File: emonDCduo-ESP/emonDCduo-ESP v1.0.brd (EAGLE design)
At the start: 99.1 x 76.5 mm, 85 parts, among them Q1 16Mhz XT49M-2016M, U1_TQFP ATMEGA328P

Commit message: updating v1.0
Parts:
- removed GPIO-4/5: (no value), SparkFun:1X02
- removed REFERENCE_SELECT: 2212S-02SG-85, SparkFun-Connectors:1X03
- removed U$1: 47219-2001_MICROSD, 47219-2001_SD_MICRO:47219-2001_MICROSD
- added GPIO5: (no value), wirepad:2,15/1,0
- added R9: 10k, rcl:R0603
- added REF_SELECT: 2212S-02SG-85, SparkFun-Connectors:1X03
- added U$2: MOLEX_MICRO_SD_1040310811, MOLEX MICRO SD [exposed pins]:MOLEX_MICROSD_EXPOSED
- REG1117: value REG1117 -> REG1117-3.3V
- TL2575HV: value TL2575HV -> TL2575HV-5V
- moved R24 2.79 mm to (79.8, 24.5)
- moved LOGO1 2.19 mm to (22.7, 15.8)
- moved C23 1.02 mm to (31.9, 56.6), turned to 0 degrees
- moved R3 0.96 mm to (42.2, 23.0), turned to 0 degrees
- moved C10 0.56 mm to (21.3, 70.1)
- moved R10 0.25 mm to (83.5, 41.9)
- renumbered 3.3V_REG to REG1117, 5V_REG to TL2575HV, C20/TUNE to C20, JP3 to JP_PWR
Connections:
- removed net N$28: REFERENCE_SELECT.2, SHUNTMON-A.6, SHUNTMON-A.7
- new net N$10: R9.2, U$2.CD1
- new net N$11: REF_SELECT.2, SHUNTMON-A.6, SHUNTMON-A.7
- net 3.3V: now also U$2.P$4; no longer U$1.PIN4
- net GND: now also REF_SELECT.3, U$2.CD2, U$2.GND1, U$2.GND2, U$2.GND3, U$2.GND4, U$2.P$6; no longer REFERENCE_SELECT.3, U$1.P$1, U$1.P$2, U$1.P$3, U$1.P$4, U$1.PIN6
- net GPIO12: now also U$2.P$7; no longer U$1.PIN7
- net GPIO13: now also U$2.P$3; no longer U$1.PIN3
- net GPIO14: now also U$2.P$5; no longer U$1.PIN5
- net GPIO2: now also U$2.P$2; no longer U$1.PIN2
- net GPIO4: now also R9.1; no longer GPIO-4/5.1
- net GPIO5: now also GPIO5.1; no longer GPIO-4/5.2
- net N$32: now also U$2.P$8; no longer U$1.PIN8
- net N$7: now also U$2.P$1; no longer U$1.PIN1
- net REFINPUT: now also REF_SELECT.1; no longer REFERENCE_SELECT.1
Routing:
- net GND: track 3.81 -> 52.3 mm, vias 54 -> 57
- net N$11: track 0.00 -> 21.4 mm, vias 0 -> 1
- net N$28: track 18.5 -> 0.00 mm, vias 1 -> 0
- net N$10: track 0.00 -> 15.8 mm, vias 0 -> 2
- net REFINPUT: track 19.4 -> 24.3 mm
- net GPIO14: track 54.8 -> 59.4 mm
- net GPIO12: track 53.6 -> 58.2 mm
- net GPIO13: track 64.9 -> 69.1 mm
- net 3.3V: track 267.5 -> 264.0 mm
- net 4.7V: track 163.5 -> 166.6 mm
- net GPIO5: track 32.0 -> 29.1 mm
- net GPIO2: track 50.0 -> 52.5 mm
- net POWERIN: track 33.6 -> 34.4 mm
- net GPIO4: track 30.5 -> 29.9 mm
- net ESPRX: track 13.1 -> 13.6 mm
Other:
- board text added: "330uH"
- board text added: "BI_DIR"
- board text added: "MicroSD"
- board text added: "UNI_DIR"
- board text added: "v1.0 Feb 2017 by DB"
- board text removed: "GPIO4"
- board text removed: "GPIO5"
- board text removed: "MICRO SD"
- board text removed: "v0.4 Jan 2017 by DB"

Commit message: update
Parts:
- added GPIO1: (no value), SparkFun:1X02
- added MINI_USB-B: 5000751517_SD, 5000751517_sd:5000751517_SD
- D1: value BAT60J -> MBRA130LT3G; device diode:SOD323_ST -> CASE 403D Diode:DO-214
- D2: value MBRA130LT3G -> BAT60J; device CASE 403D Diode:DO-214 -> diode:SOD323_ST
- moved D1 26.0 mm to (46.9, 62.4), turned to 270 degrees
- moved D2 26.0 mm to (72.8, 65.6), turned to 180 degrees
- moved GPIO0 1.14 mm to (42.2, 29.0)
- moved C11 0.25 mm to (75.0, 35.8)
- moved C4 0.25 mm to (64.8, 35.8)
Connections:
- net 4.7V: now also D2.C, FTDI1.4, MINI_USB-B.VBUS; no longer D1.C
- net 5.0V: now also D2.A; no longer D1.A
- net GND: now also D1.P$2, GPIO1.1, MINI_USB-B.GND1, MINI_USB-B.GND2, MINI_USB-B.GND3; no longer D2.P$2
- net GPIO15: now also GPIO1.2
- net IND: now also D1.P$1; no longer D2.P$1
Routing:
- net 4.7V: track 166.6 -> 186.1 mm, vias 8 -> 9
- net GPIO15: track 26.6 -> 33.3 mm
- net N$36: track 33.7 -> 31.6 mm
- net GPIO0: track 18.5 -> 19.9 mm
- net GND: vias 57 -> 59
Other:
- board text added: "D1"
- board text added: "MINI USB-B"
- board text removed: "D2"

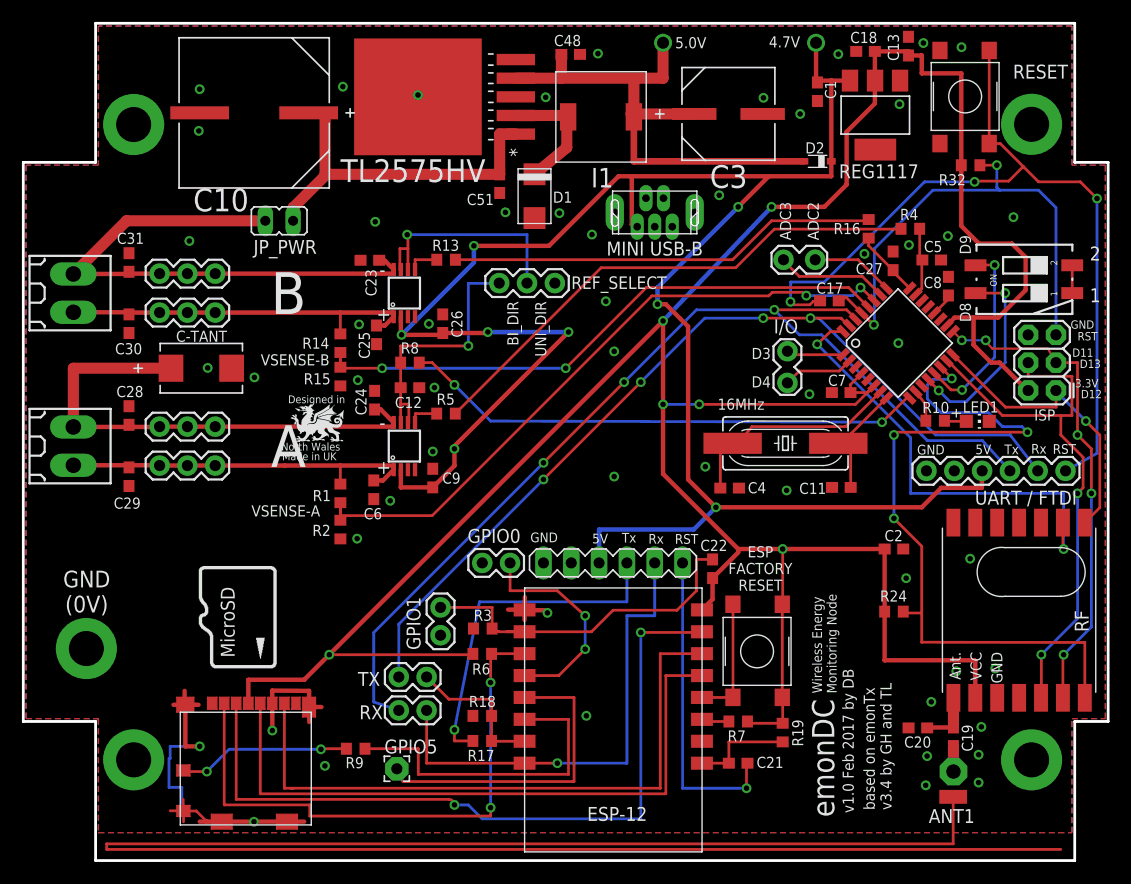
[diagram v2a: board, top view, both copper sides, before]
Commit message: added DIP switch to ESP RX/TX
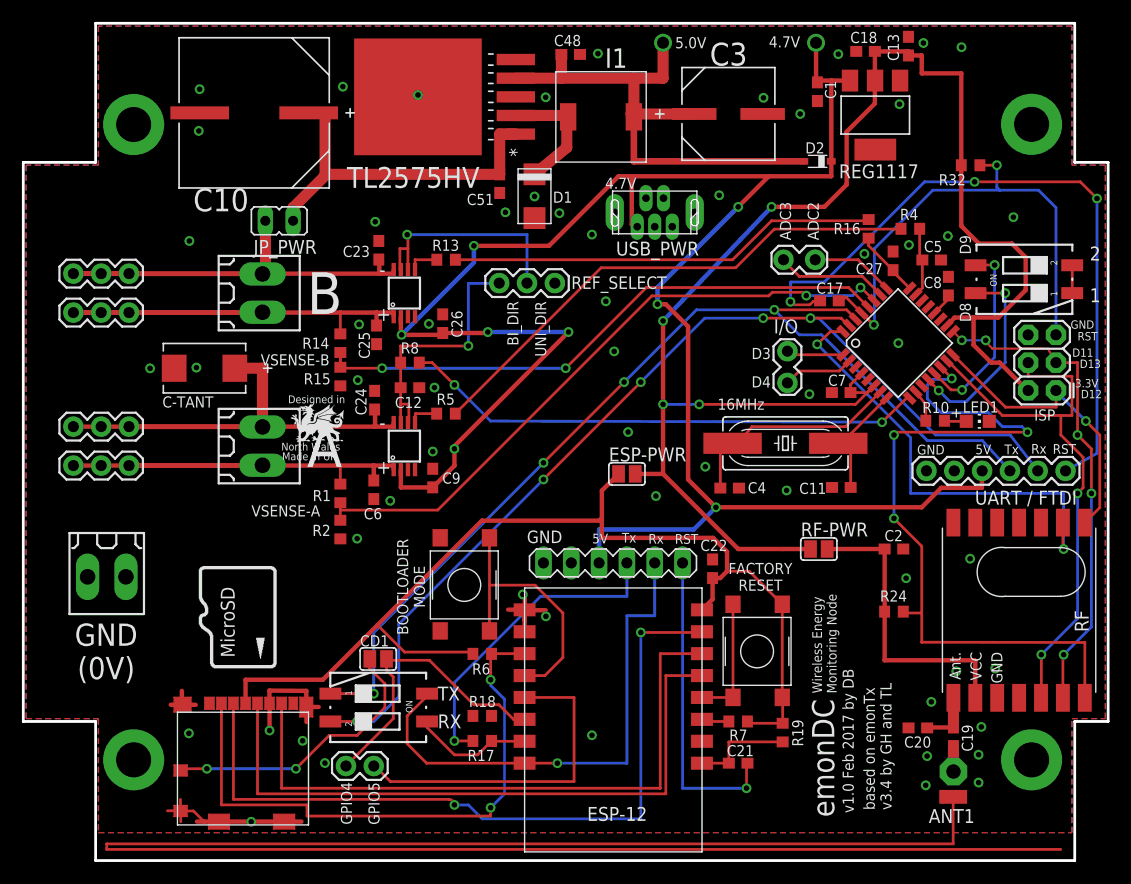
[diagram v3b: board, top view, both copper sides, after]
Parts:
- removed C28, C29, C30, C31: 0.1uF 100V, rcl:C0603
- removed GPIO0, GPIO1, RX, TX: (no value), SparkFun:1X02
- removed GPIO5: (no value), wirepad:2,15/1,0
- removed MC32882: MC32882, multicomp tact switch:SWITCH_TACT_MULTICOMP
- removed R3, R9: 10k, rcl:R0603
- added CD1, ESP-PWR, RF-PWR: (no value), jumper:SJ
- added IO2: (no value), SparkFun:1X02
- added MC2: MC32882, multicomp tact switch:SWITCH_TACT_MULTICOMP
- added S1: A6S-2104-PH, OpenEnergyMonitor:DIP_SWITCH_SMT
- added T3: (no value), con-weidmueller-sl35:180-2
- moved T1 17.3 mm to (22.1, 53.6)
- moved T2 17.3 mm to (22.1, 39.6)
- moved J1 7.87 mm to (4.83, 55.4)
- moved J2 7.87 mm to (4.83, 51.8)
- moved J3 7.87 mm to (4.83, 37.8)
- moved J4 7.87 mm to (4.83, 41.4)
- moved C23 1.22 mm to (32.7, 57.5), turned to 270 degrees
- moved C-TANT 0.29 mm to (16.8, 46.7), turned to 180 degrees
- moved U$2 0.25 mm to (20.0, 10.4)
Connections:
- net ADCVSENSE-A renamed ADC5-VSENSEB
- net ADCVSENSE-B renamed ADC4-VSENSEA
- net N$2 renamed ADC0
- net N$27 renamed ADC1
- removed net GPIO15: C22.1, ESP-12.1, ESP-12.2, GPIO1.2, R3.2
- new net 3.3V-ESP: C22.2, ESP-12.16, ESP-PWR.1, MC1.P$3, MC1.P$4, R19.2, R6.2, R7.2, U$2.P$4
- new net N$17: C2.1, R24.2, RF-PWR.2, RF.VDD
- net 3.3V: now also ESP-PWR.2, RF-PWR.1; no longer C2.1, C22.2, ESP-12.16, MC1.P$3, MC1.P$4, R19.2, R24.2, R6.2, R7.2, RF.VDD, U$2.P$4
- net ADCSHUNT-A: now also R4.2, R5.2; no longer R13.2, R16.2
- net ADCSHUNT-B: now also R13.2, R16.2; no longer R4.2, R5.2
- net D0/RX: now also S1.1; no longer RX.2
- net D1/TX: now also S1.2; no longer TX.2
- net ESPRX: now also S1.3; no longer TX.1
- net ESPTX: now also S1.4; no longer RX.1
- net GND: now also C22.1, ESP-12.1, ESP-12.2, MC2.P$1, MC2.P$2, T3.1, T3.2; no longer C28.2, C29.2, C30.2, C31.2, GPIO0.1, GPIO1.1, MC32882.P$3, MC32882.P$4, R3.1
- net GPIO0: now also MC2.P$3, MC2.P$4; no longer GPIO0.2
- net GPIO4: now also CD1.2, IO2.1; no longer R9.1
- net GPIO5: now also IO2.2; no longer GPIO5.1
- net INPUT-POS-A: no longer C30.1
- net INPUT-POS-B: no longer C29.1
- net LOAD-NEG-A: no longer C31.1
- net LOAD-NEG-B: no longer C28.1
- net N$10: now also CD1.1; no longer R9.2
- net RES: no longer MC32882.P$1, MC32882.P$2
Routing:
- net 3.3V: track 264.0 -> 144.9 mm, vias 6 -> 4
- net 3.3V-ESP: track 0.00 -> 96.2 mm
- net GPIO15: track 33.3 -> 0.00 mm
- net N$17: track 0.00 -> 27.1 mm
- net INPUT-POS-A: track 33.5 -> 50.3 mm
- net RES: track 77.6 -> 63.9 mm
- net GND: track 52.3 -> 39.8 mm, vias 59 -> 62
- net INPUT-POS-B: track 33.7 -> 44.9 mm
- net N$10: track 15.8 -> 26.1 mm
- net D1/TX: track 84.6 -> 93.6 mm, vias 4 -> 5
- net ADCSHUNT-B: track 47.7 -> 39.3 mm
- net ADCSHUNT-A: track 39.3 -> 47.7 mm
- net LOAD-NEG-B: track 48.4 -> 56.5 mm
- net GPIO0: track 19.9 -> 24.5 mm, vias 2 -> 0
- net ESPTX: track 43.9 -> 47.3 mm
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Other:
- board text added: "BOOTLOADER MODE"
- board text added: "FACTORY RESET"
- board text added: "Format MicroSD card to FAT32. Place blank 'datalog.txt' file there."
- board text added: "GPIO4"
- board text added: "GPIO5"
- board text added: "RX"
- board text added: "TX"
- board text added: "USB_PWR"
- board text removed: "ESP FACTORY RESET"
- board text removed: "MINI USB-B"
- board text removed: "RESET"

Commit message: emonBIKE v0.2 camexport
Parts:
- removed C-TANT: 10uF 63V, 2917 footprint capacitor:2917
- removed C17: 100nF, rcl:C0603
- removed JP_PWR: 2211S-02G, jumper:JP1
- removed MC1: MC32882, multicomp tact switch:SWITCH_TACT_MULTICOMP
- removed REF_SELECT: 2212S-02SG-85, SparkFun-Connectors:1X03
- added C14, C15: 100nF, rcl:C0603
- added C16: 0.1uF 100V, rcl:C0603
- added IO1: (no value), SparkFun:1X02
- added PWR: (no value), SparkFun-Connectors:1X03
- added REF_GND: (no value), jumper:SJ
- added REF_SELECT_A: 2212S-02SG-85, SparkFun-Connectors:1X03
- C12: value 220nF -> 100nF
- C26, C9: value 0.1uF 100V -> 100nF
- C3: value 470uF -> 470uF 16V
- C51: value 100nF -> 0.1uF 100V
- R1, R14: value 100K 60V -> 100K 75V
- R15, R2: value 5.9K -> 5.6K
- R17: value 5.6k -> 5.6K
- R18, R19, R6, R7: value 10k -> 10K
- R32: value 10K -> 10k
- moved RF-PWR 17.1 mm to (56.9, 36.3)
- moved R8 12.5 mm to (46.2, 53.8), turned to 270 degrees
- moved C12 11.4 mm to (42.7, 53.8), turned to 270 degrees
- moved IO2 5.34 mm to (32.0, 5.59)
- moved ESP-PWR 3.05 mm to (55.4, 40.1)
- moved S3 2.81 mm to (91.6, 57.7)
- moved C51 0.51 mm to (44.3, 63.6)
- moved R18 0.36 mm to (42.4, 14.7)
- moved CD1 0.25 mm to (32.7, 20.4)
- moved R17 0.25 mm to (42.4, 12.7)
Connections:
- net N$17 renamed 3.3V-RF
- removed net INPUT-POS-A: C25.1, J2.1, J2.2, J2.3, R14.2, SHUNTMON-A.1, T1.2
- removed net INPUT-POS-B: C6.1, J3.1, J3.2, J3.3, R1.2, SHUNTMON-B.1, T2.2
- removed net POWERIN: C10.1, C51.1, JP_PWR.1, TL2575HV.1
- removed net RES: C17.1, FTDI/UART.DTR
- removed net RESET: C17.2, ISP.5, R32.1, U1_TQFP.29
- new net PWR_IN: C10.1, C16.1, C51.1, PWR.2, TL2575HV.1
- new net RESET1: C14.2, FTDI/UART.DTR, ISP.5
- new net RESET2: C14.1, R32.1, U1_TQFP.29
- new net SOURCE-POS-A: C6.1, J3.1, J3.2, J3.3, PWR.1, R1.2, SHUNTMON-B.1, T2.2
- new net SOURCE-POS-B: C25.1, J2.1, J2.2, J2.3, PWR.3, R14.2, SHUNTMON-A.1, T1.2
- net 3.3V-ESP: now also IO1.2; no longer MC1.P$3, MC1.P$4
- net GND: now also C15.2, C16.2, REF_GND.2, REF_SELECT_A.3; no longer C-TANT.2, REF_SELECT.3
- net GPIO16: now also IO1.1; no longer MC1.P$1, MC1.P$2
- net LOAD-NEG-A: now also C24.2, J4.1, J4.2, J4.3, SHUNTMON-B.8, T2.1; no longer C23.2, J1.1, J1.2, J1.3, JP_PWR.2, SHUNTMON-A.8, T1.1
- net LOAD-NEG-B: now also C23.2, J1.1, J1.2, J1.3, SHUNTMON-A.8, T1.1; no longer C-TANT.1, C24.2, J4.1, J4.2, J4.3, SHUNTMON-B.8, T2.1
- net N$11: now also REF_SELECT_A.2, SHUNTMON-B.6, SHUNTMON-B.7; no longer REF_SELECT.2, SHUNTMON-A.6, SHUNTMON-A.7
- net REFINPUT: now also C15.1, REF_GND.1, REF_SELECT_A.1, SHUNTMON-A.6, SHUNTMON-A.7; no longer REF_SELECT.1, SHUNTMON-B.6, SHUNTMON-B.7
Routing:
- net SOURCE-POS-A: track 0.00 -> 76.1 mm
- net SOURCE-POS-B: track 0.00 -> 64.8 mm
- net RES: track 63.9 -> 0.00 mm, vias 3 -> 0
- net INPUT-POS-A: track 50.3 -> 0.00 mm
- net PWR_IN: track 0.00 -> 49.5 mm
- net RESET: track 46.3 -> 0.00 mm, vias 2 -> 0
- net INPUT-POS-B: track 44.9 -> 0.00 mm
- net POWERIN: track 34.4 -> 0.00 mm
- net RESET1: track 0.00 -> 29.2 mm
- net RESET2: track 0.00 -> 21.7 mm, vias 0 -> 2
- net 3.3V: track 144.9 -> 125.5 mm
- net 3.3V-RF: track 27.1 -> 45.6 mm
- net N$11: track 21.4 -> 8.98 mm, vias 1 -> 0
- net REFINPUT: track 24.3 -> 35.3 mm, vias 1 -> 2
- net LOAD-NEG-B: track 56.5 -> 48.9 mm
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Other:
- board text added: "BI"
- board text added: "UART/FTDI"
- board text added: "UNI"
- board text removed: "BI_DIR"
- board text removed: "UART / FTDI"
- board text removed: "UNI_DIR"
